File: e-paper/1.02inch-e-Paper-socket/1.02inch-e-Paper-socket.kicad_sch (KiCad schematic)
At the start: 2 parts, among them J1 Conn_01x06_Pin, J2 Conn_01x03_Pin

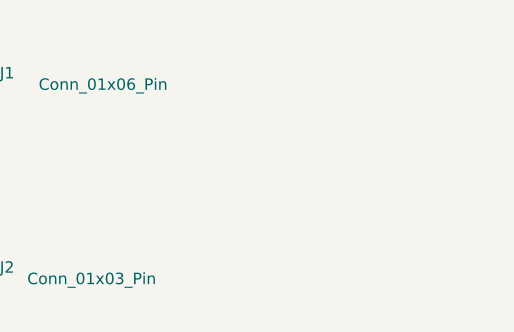
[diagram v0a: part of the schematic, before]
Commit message: update e-paper boundary
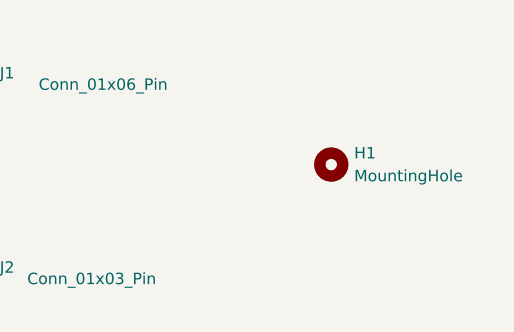
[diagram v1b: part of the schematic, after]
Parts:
- added H1: MountingHole, ErgoCai.pretty:e-paper_1.02inch_mount, symbol Mechanical:MountingHole
- J1: footprint Connector_PinSocket_2.54mm:PinSocket_1x05_P2.54mm_Vertical -> ErgoCai.pretty:PinSocket_1x05_P2.54mm_Vertical
- J2: footprint Connector_PinSocket_2.54mm:PinSocket_1x03_P2.54mm_Vertical -> ErgoCai.pretty:PinSocket_1x03_P2.54mm_Vertical
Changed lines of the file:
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@@
 			)
 		)
-		(property "Footprint" "Connector_PinSocket_2.54mm:PinSocket_1x03_P2.54mm_Vertical"
+		(property "Footprint" "ErgoCai.pretty:PinSocket_1x03_P2.54mm_Vertical"
 			(at 109.22 93.98 0)
 			(effects
@@
 			)
 		)
-		(property "Footprint" "Connector_PinSocket_2.54mm:PinSocket_1x05_P2.54mm_Vertical"
+		(property "Footprint" "ErgoCai.pretty:PinSocket_1x05_P2.54mm_Vertical"
 			(at 109.22 72.39 0)
 			(effects
@@
 					(unit 1)
 				)
+			)
+		)
+	)
+	(symbol
+		(lib_id "Mechanical:MountingHole")
+		(at 147.32 81.28 0)
+		(unit 1)
+		(exclude_from_sim no)
+		(in_bom no)
+		(on_board yes)
+		(dnp no)
+		(fields_autoplaced yes)
+		(property "Reference" "H1"
+			(at 149.86 80.0099 0)
+			(effects
+				(font
+					(size 1.27 1.27)
+				)
+				(justify left)
+			)
+		)
+		(property "Value" "MountingHole"
+			(at 149.86 82.5499 0)
+			(effects
+				(font
+					(size 1.27 1.27)
+				)
+				(justify left)
+			)
+		)
+		(property "Footprint" "ErgoCai.pretty:e-paper_1.02inch_mount"
+			(at 147.32 81.28 0)
+			(effects
+				(font
+					(size 1.27 1.27)
+				)
+				(hide yes)
+			)
+		)
+		(property "Datasheet" "~"
+			(at 147.32 81.28 0)
+			(effects
+				(font
+					(size 1.27 1.27)
+				)
+				(hide yes)
+			)
+		)
+		(property "Description" "Mounting Hole without connection"
+			(at 147.32 81.28 0)
+			(effects
+				(font
+					(size 1.27 1.27)
+				)
+				(hide yes)
+			)
+		)
+		(instances
+			(project ""
+				(path "/dcbfc6a7-a2a9-4110-89bd-d7cd283ac454"
+					(reference "H1")
+					(unit 1)
+				)

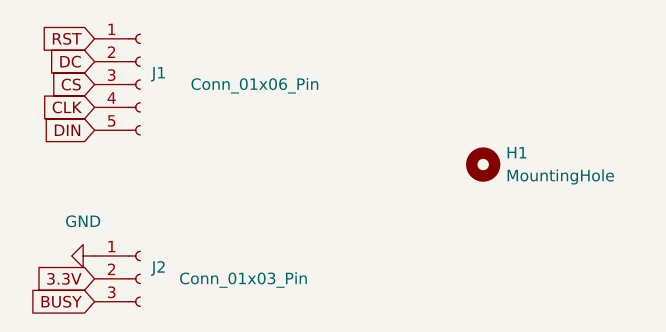
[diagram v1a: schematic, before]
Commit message: update reference in joystick and e-paper
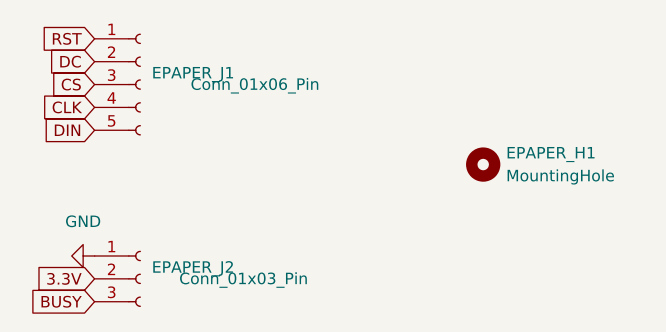
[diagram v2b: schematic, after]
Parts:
- renumbered H1 to EPAPER_H1, J1 to EPAPER_J1, J2 to EPAPER_J2
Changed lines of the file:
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@@
 		(on_board yes)
 		(dnp no)
-		(property "Reference" "J2"
+		(property "Reference" "EPAPER_J2"
 			(at 110.49 92.7099 0)
 			(effects
@@
 			(project "1.02inch-e-Paper-socket"
 				(path "/dcbfc6a7-a2a9-4110-89bd-d7cd283ac454"
-					(reference "J2")
+					(reference "EPAPER_J2")
 					(unit 1)
 				)
@@
 		(on_board yes)
 		(dnp no)
-		(property "Reference" "J1"
+		(property "Reference" "EPAPER_J1"
 			(at 110.49 71.1199 0)
 			(effects
@@
 			(project "1.02inch-e-Paper-socket"
 				(path "/dcbfc6a7-a2a9-4110-89bd-d7cd283ac454"
-					(reference "J1")
+					(reference "EPAPER_J1")
 					(unit 1)
 				)
@@
 		(dnp no)
 		(fields_autoplaced yes)
-		(property "Reference" "H1"
+		(property "Reference" "EPAPER_H1"
 			(at 149.86 80.0099 0)
 			(effects
@@
 			(project ""
 				(path "/dcbfc6a7-a2a9-4110-89bd-d7cd283ac454"
-					(reference "H1")
-					(unit 1)
-				)
+					(reference "EPAPER_H1")
+					(unit 1)
+				)

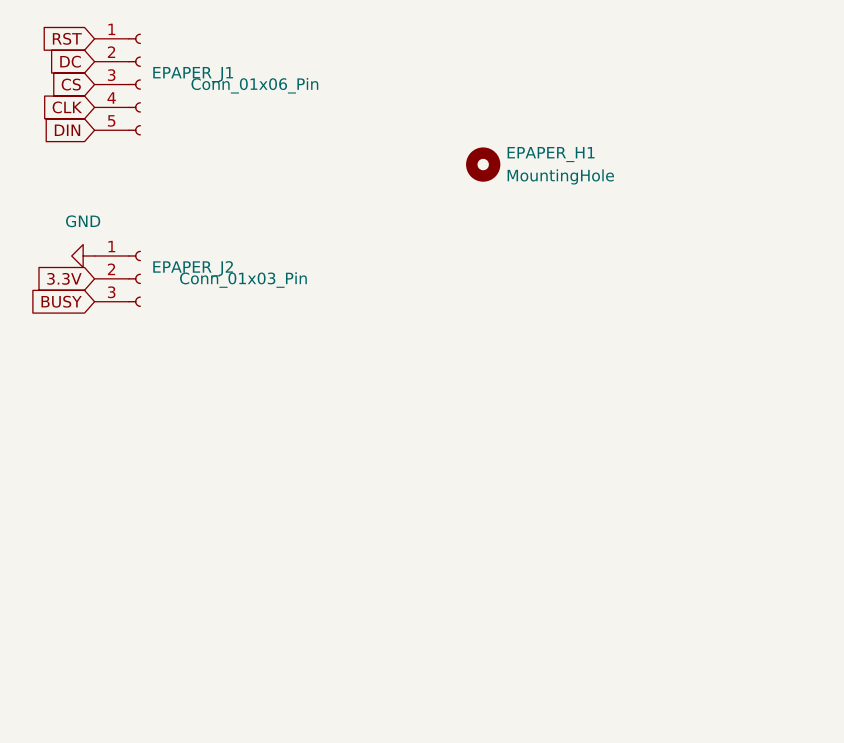
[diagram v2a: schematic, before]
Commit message: use 10pin connector socket instead of 9
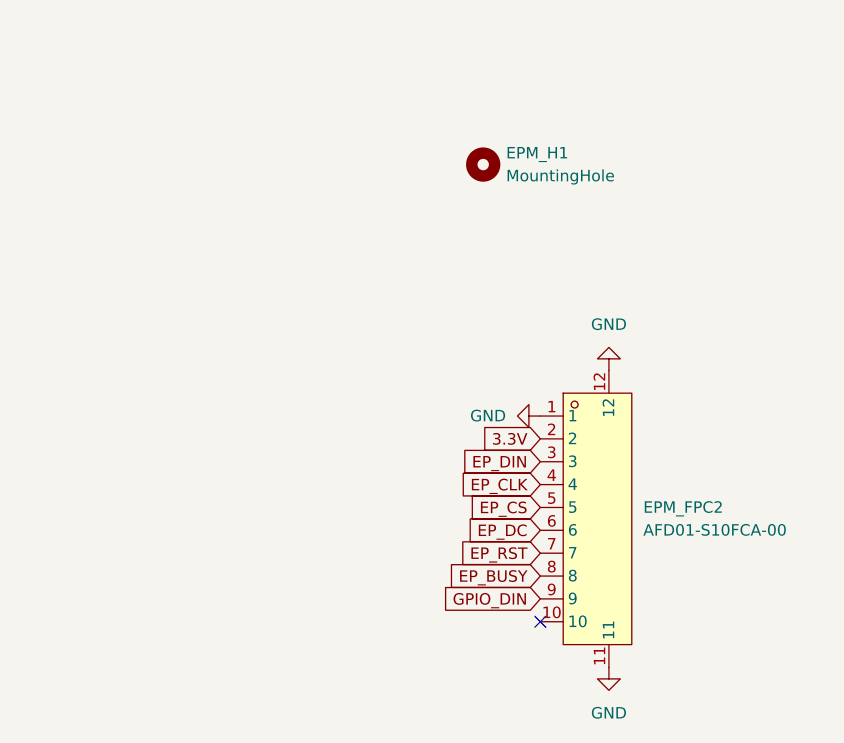
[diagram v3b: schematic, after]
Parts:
- removed EPAPER_J1: Conn_01x06_Pin, ErgoCai.pretty:PinSocket_1x05_P2.54mm_Vertical, symbol Connector:Conn_01x05_Socket
- removed EPAPER_J2: Conn_01x03_Pin, ErgoCai.pretty:PinSocket_1x03_P2.54mm_Vertical, symbol Connector:Conn_01x03_Socket
- added EPM_FPC2: AFD01-S10FCA-00, ErgoCai.pretty:FPC-SMD_10P-P0.50_JS_AFD01-S10FCA-00, symbol ErgoCai:AFD01-S10FCA-00
- renumbered EPAPER_H1 to EPM_H1
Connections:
- net 3.3V: now also EPM_FPC2.2
- net GND: now also EPM_FPC2.1, EPM_FPC2.11, EPM_FPC2.12
- new net EP_BUSY: EPM_FPC2.8
- new net EP_CLK: EPM_FPC2.4
- new net EP_CS: EPM_FPC2.5
- new net EP_DC: EPM_FPC2.6
- new net EP_DIN: EPM_FPC2.3
- new net EP_RST: EPM_FPC2.7
- new net GPIO_DIN: EPM_FPC2.9
- no-connect marks 0 -> 1

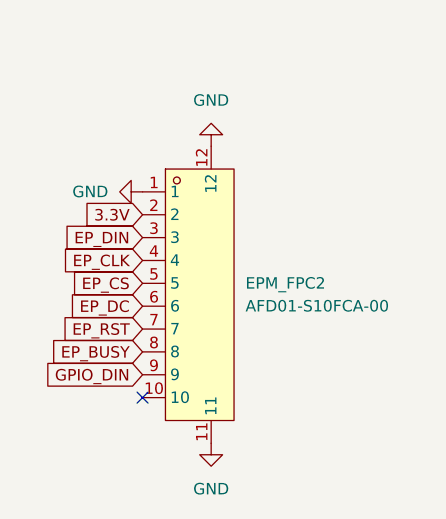
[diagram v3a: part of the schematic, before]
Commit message: updat e-paper module
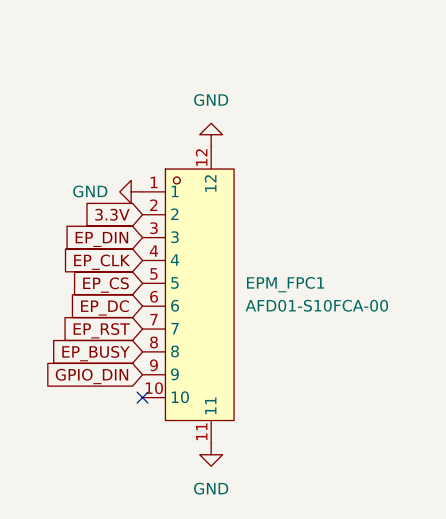
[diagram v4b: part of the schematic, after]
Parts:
- renumbered EPM_FPC2 to EPM_FPC1
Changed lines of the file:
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@@
 		(dnp no)
 		(fields_autoplaced yes)
-		(property "Reference" "EPM_FPC2"
+		(property "Reference" "EPM_FPC1"
 			(at 165.1 119.3799 0)
 			(effects
@@
 			(project "1.02inch-e-Paper-socket"
 				(path "/dcbfc6a7-a2a9-4110-89bd-d7cd283ac454"
-					(reference "EPM_FPC2")
+					(reference "EPM_FPC1")
 					(unit 1)
 				)
